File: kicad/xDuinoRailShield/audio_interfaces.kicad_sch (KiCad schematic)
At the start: 5 parts, among them J2 AudioJack2_Ground, J8 Conn_01x04, J9 Conn_01x05

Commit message: More busses added
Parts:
- renumbered C9 to C301, J2 to J301, J8 to J302, J9 to J303, RV1 to RV301
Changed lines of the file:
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@@
 		(dnp no)
 		(fields_autoplaced yes)
-		(property "Reference" "#PWR031"
+		(property "Reference" "#PWR0304"
 			(at 91.44 67.31 0)
 			(effects
@@
 			(project "xDuinoRailShield"
 				(path "/e63e39d7-6ac0-4ffd-8aa3-1841a4541b55/89db4163-62dc-424d-9343-e2bee6963b15"
-					(reference "#PWR031")
+					(reference "#PWR0304")
 					(unit 1)
 				)
@@
 		(on_board yes)
 		(dnp no)
-		(property "Reference" "RV1"
+		(property "Reference" "RV301"
 			(at 93.98 50.7999 0)
 			(effects
@@
 			(project "xDuinoRailShield"
 				(path "/e63e39d7-6ac0-4ffd-8aa3-1841a4541b55/89db4163-62dc-424d-9343-e2bee6963b15"
-					(reference "RV1")
+					(reference "RV301")
 					(unit 1)
 				)
@@
 		(on_board yes)
 		(dnp no)
-		(property "Reference" "J2"
+		(property "Reference" "J301"
 			(at 55.245 43.18 0)
 			(effects
@@
 			(project "xDuinoRailShield"
 				(path "/e63e39d7-6ac0-4ffd-8aa3-1841a4541b55/89db4163-62dc-424d-9343-e2bee6963b15"
-					(reference "J2")
+					(reference "J301")
 					(unit 1)
 				)
@@
 		(dnp no)
 		(fields_autoplaced yes)
-		(property "Reference" "#PWR029"
+		(property "Reference" "#PWR0301"
 			(at 55.88 67.31 0)
 			(effects
@@
 			(project "xDuinoRailShield"
 				(path "/e63e39d7-6ac0-4ffd-8aa3-1841a4541b55/89db4163-62dc-424d-9343-e2bee6963b15"
-					(reference "#PWR029")
+					(reference "#PWR0301")
 					(unit 1)
 				)
@@
 		(dnp no)
 		(fields_autoplaced yes)
-		(property "Reference" "#PWR030"
+		(property "Reference" "#PWR0302"
 			(at 73.66 50.8 0)
 			(effects
@@
 			(project "xDuinoRailShield"
 				(path "/e63e39d7-6ac0-4ffd-8aa3-1841a4541b55/89db4163-62dc-424d-9343-e2bee6963b15"
-					(reference "#PWR030")
+					(reference "#PWR0302")
 					(unit 1)
 				)
@@
 		(dnp no)
 		(fields_autoplaced yes)
-		(property "Reference" "#PWR038"
+		(property "Reference" "#PWR0303"
 			(at 78.74 123.19 0)
 			(effects
@@
 			(project "xDuinoRailShield"
 				(path "/e63e39d7-6ac0-4ffd-8aa3-1841a4541b55/89db4163-62dc-424d-9343-e2bee6963b15"
-					(reference "#PWR038")
+					(reference "#PWR0303")
 					(unit 1)
 				)
@@
 		(dnp no)
 		(fields_autoplaced yes)
-		(property "Reference" "#PWR039"
+		(property "Reference" "#PWR0305"
 			(at 157.48 125.73 0)
 			(effects
@@
 			(project "xDuinoRailShield"
 				(path "/e63e39d7-6ac0-4ffd-8aa3-1841a4541b55/89db4163-62dc-424d-9343-e2bee6963b15"
-					(reference "#PWR039")
+					(reference "#PWR0305")
 					(unit 1)
 				)
@@
 		(on_board yes)
 		(dnp no)
-		(property "Reference" "C9"
+		(property "Reference" "C301"
 			(at 83.439 44.45 90)
 			(effects
@@
 			(project "xDuinoRailShield"
 				(path "/e63e39d7-6ac0-4ffd-8aa3-1841a4541b55/89db4163-62dc-424d-9343-e2bee6963b15"
-					(reference "C9")
+					(reference "C301")
 					(unit 1)
 				)
@@
 		(on_board yes)
 		(dnp no)
-		(property "Reference" "J9"
+		(property "Reference" "J303"
 			(at 144.78 107.9499 0)
 			(effects
@@
 			(project "xDuinoRailShield"
 				(path "/e63e39d7-6ac0-4ffd-8aa3-1841a4541b55/89db4163-62dc-424d-9343-e2bee6963b15"
-					(reference "J9")
+					(reference "J303")
 					(unit 1)
 				)
@@
 		(on_board yes)
 		(dnp no)
-		(property "Reference" "J8"
+		(property "Reference" "J302"
 			(at 66.04 109.2201 0)
 			(effects
@@
 			(project "xDuinoRailShield"
 				(path "/e63e39d7-6ac0-4ffd-8aa3-1841a4541b55/89db4163-62dc-424d-9343-e2bee6963b15"
-					(reference "J8")
-					(unit 1)
-				)
+					(reference "J302")
+					(unit 1)
+				)

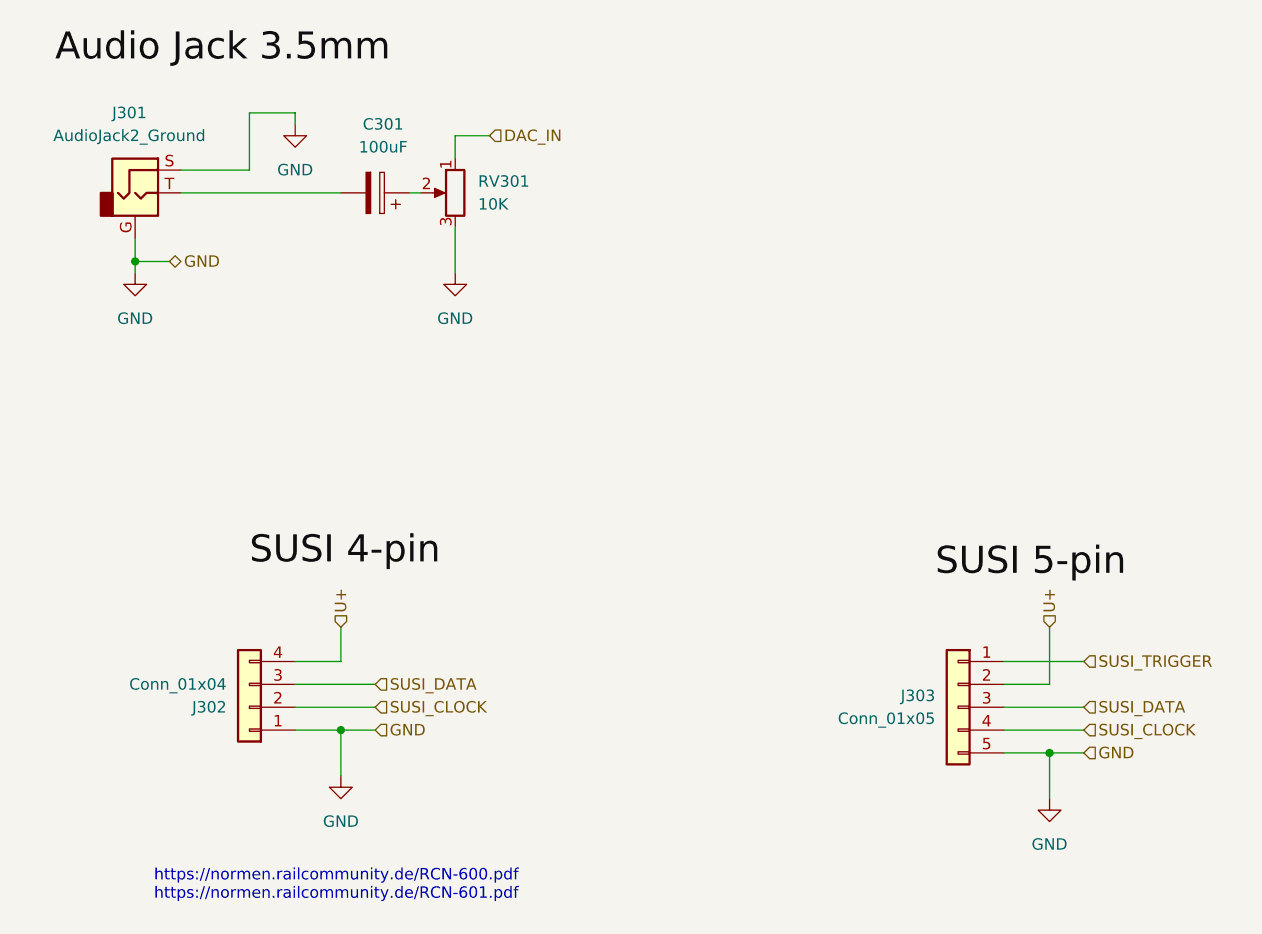
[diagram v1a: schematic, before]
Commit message: Draft of loco decoder
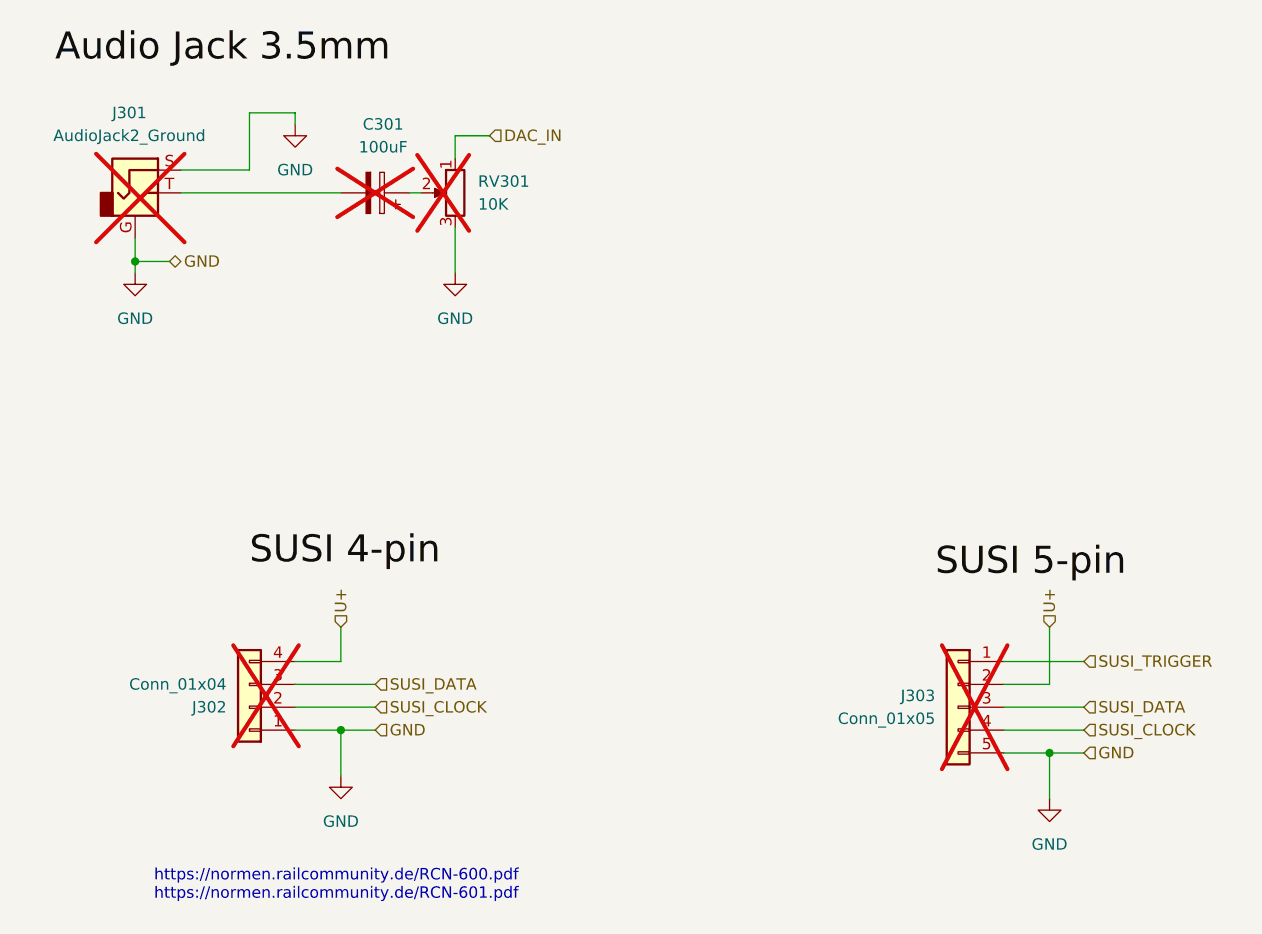
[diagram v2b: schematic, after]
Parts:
- C301, J301, J302, J303, RV301: now not fitted; now left out of the parts list
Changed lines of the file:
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@@
 		(mirror y)
 		(unit 1)
-		(exclude_from_sim no)
-		(in_bom yes)
-		(on_board yes)
-		(dnp no)
+		(exclude_from_sim yes)
+		(in_bom no)
+		(on_board no)
+		(dnp yes)
 		(property "Reference" "RV301"
 			(at 93.98 50.7999 0)
@@
 			)
 		)
+		(property "Field-1" ""
+			(at 91.44 52.07 0)
+			(effects
+				(font
+					(size 1.27 1.27)
+				)
+				(hide yes)
+			)
+		)
 		(pin "3"
 		)
@@
 		(at 55.88 52.07 0)
 		(unit 1)
-		(exclude_from_sim no)
-		(in_bom yes)
-		(on_board yes)
-		(dnp no)
+		(exclude_from_sim yes)
+		(in_bom no)
+		(on_board no)
+		(dnp yes)
 		(property "Reference" "J301"
 			(at 55.245 43.18 0)
@@
 		)
 		(property "Description" "Audio Jack, 2 Poles (Mono / TS), Grounded Sleeve"
+			(at 55.88 52.07 0)
+			(effects
+				(font
+					(size 1.27 1.27)
+				)
+				(hide yes)
+			)
+		)
+		(property "Field-1" ""
 			(at 55.88 52.07 0)
 			(effects
@@
 		(mirror x)
 		(unit 1)
-		(exclude_from_sim no)
-		(in_bom yes)
-		(on_board yes)
-		(dnp no)
+		(exclude_from_sim yes)
+		(in_bom no)
+		(on_board no)
+		(dnp yes)
 		(property "Reference" "C301"
 			(at 83.439 44.45 90)
@@
 		)
 		(property "Description" "Polarized capacitor"
+			(at 82.55 52.07 0)
+			(effects
+				(font
+					(size 1.27 1.27)
+				)
+				(hide yes)
+			)
+		)
+		(property "Field-1" ""
 			(at 82.55 52.07 0)
 			(effects
@@
 		(mirror y)
 		(unit 1)
-		(exclude_from_sim no)
-		(in_bom yes)
-		(on_board yes)
-		(dnp no)
+		(exclude_from_sim yes)
+		(in_bom no)
+		(on_board no)
+		(dnp yes)
 		(property "Reference" "J303"
 			(at 144.78 107.9499 0)
@@
 			)
 		)
+		(property "Field-1" ""
+			(at 147.32 109.22 0)
+			(effects
+				(font
+					(size 1.27 1.27)
+				)
+				(hide yes)
+			)
+		)
 		(pin "1"
 		)
@@
 		(at 68.58 109.22 180)
 		(unit 1)
-		(exclude_from_sim no)
-		(in_bom yes)
-		(on_board yes)
-		(dnp no)
+		(exclude_from_sim yes)
+		(in_bom no)
+		(on_board no)
+		(dnp yes)
 		(property "Reference" "J302"
 			(at 66.04 109.2201 0)
@@
 			(at 68.58 109.22 0)
 			(effects
+				(font
+					(size 1.27 1.27)
+				)
+				(hide yes)
+			)
+		)
+		(property "Field-1" ""
+			(at 68.58 109.22 0)
+			(effects

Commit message: A lot of fixes
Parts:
- renumbered C301 to C201, J301 to J201, J302 to J202, J303 to J203, RV301 to RV201
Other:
- note added: "Audio Jack 3.5mm"
- note added: "SUSI 4-pin"
- note added: "SUSI 5-pin"
- company: (none) -> Chatelain Engineering
- title: (none) -> DCC Bus Input
- moved on the sheet: J202
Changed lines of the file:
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@@
 	(generator_version "7.99")
 	(paper "A4")
+	(title_block
+		(title "DCC Bus Input")
+		(date "2024-01-03")
+		(rev "v0.1")
+		(company "Chatelain Engineering")
+	)
 	(junction
-		(at 78.74 111.76)
+		(at 71.12 113.03)
 		(diameter 0)
 		(color 0 0 0 0)
@@
 	(wire
 		(pts
-			(xy 78.74 100.33) (xy 78.74 104.14)
+			(xy 71.12 101.6) (xy 71.12 105.41)
 		)
 		(stroke
@@
 	(wire
 		(pts
-			(xy 78.74 111.76) (xy 78.74 116.84)
+			(xy 71.12 113.03) (xy 71.12 118.11)
 		)
 		(stroke
@@
 	(wire
 		(pts
-			(xy 78.74 111.76) (xy 82.55 111.76)
-		)
-		(stroke
-			(width 0)
-			(type default)
-		)
-	)
-	(wire
-		(pts
-			(xy 82.55 106.68) (xy 73.66 106.68)
-		)
-		(stroke
-			(width 0)
-			(type default)
-		)
-	)
-	(wire
-		(pts
-			(xy 73.66 104.14) (xy 78.74 104.14)
+			(xy 71.12 113.03) (xy 74.93 113.03)
+		)
+		(stroke
+			(width 0)
+			(type default)
+		)
+	)
+	(wire
+		(pts
+			(xy 74.93 107.95) (xy 66.04 107.95)
+		)
+		(stroke
+			(width 0)
+			(type default)
+		)
+	)
+	(wire
+		(pts
+			(xy 66.04 105.41) (xy 71.12 105.41)
 		)
 		(stroke
@@
 	(wire
 		(pts
-			(xy 82.55 109.22) (xy 73.66 109.22)
+			(xy 74.93 110.49) (xy 66.04 110.49)
 		)
 		(stroke
@@
 	(wire
 		(pts
-			(xy 73.66 111.76) (xy 78.74 111.76)
-		)
-		(stroke
-			(width 0)
-			(type default)
+			(xy 66.04 113.03) (xy 71.12 113.03)
+		)
+		(stroke
+			(width 0)
+			(type default)
+		)
+	)
+	(text "SUSI 5-pin"
+		(exclude_from_sim no)
+		(at 157.48 93.472 0)
+		(effects
+			(font
+				(size 3.048 3.048)
+			)
+		)
+	)
+	(text "SUSI 4-pin"
+		(exclude_from_sim no)
+		(at 73.66 93.726 0)
+		(effects
+			(font
+				(size 3.048 3.048)
+			)
 		)
 	)
 	(text "https://normen.railcommunity.de/RCN-600.pdf\nhttps://normen.railcommunity.de/RCN-601.pdf"
 		(exclude_from_sim no)
-		(at 78.232 129.032 0)
+		(at 70.612 130.302 0)
 		(effects
 			(font
@@
 		)
 	)
-	(label "Audio Jack 3.5mm"
-		(at 46.99 38.1 0)
-		(fields_autoplaced yes)
-		(effects
-			(font
-				(size 3 3)
-			)
-			(justify left bottom)
-		)
-	)
-	(label "SUSI 4-pin"
-		(at 68.58 93.98 0)
-		(fields_autoplaced yes)
-		(effects
-			(font
-				(size 3 3)
-			)
-			(justify left bottom)
-		)
-	)
-	(label "SUSI 5-pin"
-		(at 144.78 95.25 0)
-		(fields_autoplaced yes)
-		(effects
-			(font
-				(size 3 3)
-			)
-			(justify left bottom)
+	(text "Audio Jack 3.5mm"
+		(exclude_from_sim no)
+		(at 77.216 36.83 0)
+		(effects
+			(font
+				(size 3.048 3.048)
+			)
 		)
 	)
 	(hierarchical_label "SUSI_CLOCK"
 		(shape input)
-		(at 82.55 109.22 0)
+		(at 74.93 110.49 0)
 		(fields_autoplaced yes)
 		(effects
@@
 	(hierarchical_label "U+"
 		(shape input)
-		(at 78.74 100.33 90)
+		(at 71.12 101.6 90)
 		(fields_autoplaced yes)
 		(effects
@@
 	(hierarchical_label "GND"
 		(shape input)
-		(at 82.55 111.76 0)
+		(at 74.93 113.03 0)
 		(fields_autoplaced yes)
 		(effects
@@
 	(hierarchical_label "SUSI_DATA"
 		(shape input)
-		(at 82.55 106.68 0)
+		(at 74.93 107.95 0)
 		(fields_autoplaced yes)
 		(effects
@@
 		(dnp no)
 		(fields_autoplaced yes)
-		(property "Reference" "#PWR0304"
+		(property "Reference" "#PWR0204"
 			(at 91.44 67.31 0)
 			(effects
@@
 			(project "xDuinoRailShield"
 				(path "/e63e39d7-6ac0-4ffd-8aa3-1841a4541b55/89db4163-62dc-424d-9343-e2bee6963b15"
-					(reference "#PWR0304")
+					(reference "#PWR0204")
 					(unit 1)
 				)
@@
 		(on_board no)
 		(dnp yes)
-		(property "Reference" "RV301"
+		(property "Reference" "RV201"
 			(at 93.98 50.7999 0)
 			(effects
@@
 			(project "xDuinoRailShield"
 				(path "/e63e39d7-6ac0-4ffd-8aa3-1841a4541b55/89db4163-62dc-424d-9343-e2bee6963b15"
-					(reference "RV301")
+					(reference "RV201")
 					(unit 1)
 				)
@@
 		(on_board no)
 		(dnp yes)
-		(property "Reference" "J301"
+		(property "Reference" "J201"
 			(at 55.245 43.18 0)
 			(effects
@@
 			(project "xDuinoRailShield"
 				(path "/e63e39d7-6ac0-4ffd-8aa3-1841a4541b55/89db4163-62dc-424d-9343-e2bee6963b15"
-					(reference "J301")
+					(reference "J201")
 					(unit 1)
 				)
@@
 		(dnp no)
 		(fields_autoplaced yes)
-		(property "Reference" "#PWR0301"
+		(property "Reference" "#PWR0201"
 			(at 55.88 67.31 0)
 			(effects
@@
 			(project "xDuinoRailShield"
 				(path "/e63e39d7-6ac0-4ffd-8aa3-1841a4541b55/89db4163-62dc-424d-9343-e2bee6963b15"
-					(reference "#PWR0301")
+					(reference "#PWR0201")
 					(unit 1)
 				)
@@
 		(dnp no)
 		(fields_autoplaced yes)
-		(property "Reference" "#PWR0302"
+		(property "Reference" "#PWR0202"
 			(at 73.66 50.8 0)
 			(effects
@@
 			(project "xDuinoRailShield"
 				(path "/e63e39d7-6ac0-4ffd-8aa3-1841a4541b55/89db4163-62dc-424d-9343-e2bee6963b15"
-					(reference "#PWR0302")
+					(reference "#PWR0202")
 					(unit 1)
 				)
@@
 	(symbol
 		(lib_id "power:GND")
-		(at 78.74 116.84 0)
+		(at 71.12 118.11 0)
 		(unit 1)
 		(exclude_from_sim no)
@@
 		(dnp no)
 		(fields_autoplaced yes)
-		(property "Reference" "#PWR0303"
-			(at 78.74 123.19 0)
+		(property "Reference" "#PWR0203"
+			(at 71.12 124.46 0)
 			(effects
 				(font
@@
 		)
 		(property "Value" "GND"
-			(at 78.74 121.92 0)
+			(at 71.12 123.19 0)
 			(effects
 				(font
@@
 		)
 		(property "Footprint" ""
-			(at 78.74 116.84 0)
+			(at 71.12 118.11 0)
 			(effects
 				(font
@@
 		)
 		(property "Datasheet" ""
-			(at 78.74 116.84 0)
+			(at 71.12 118.11 0)
 			(effects
 				(font
@@
 		)
 		(property "Description" "Power symbol creates a global label with name \"GND\" , ground"
-			(at 78.74 116.84 0)
+			(at 71.12 118.11 0)
 			(effects
 				(font
@@
 			(project "xDuinoRailShield"
 				(path "/e63e39d7-6ac0-4ffd-8aa3-1841a4541b55/89db4163-62dc-424d-9343-e2bee6963b15"
-					(reference "#PWR0303")
+					(reference "#PWR0203")
 					(unit 1)
 				)
@@
 		(dnp no)
 		(fields_autoplaced yes)
-		(property "Reference" "#PWR0305"
+		(property "Reference" "#PWR0205"
 			(at 157.48 125.73 0)
 			(effects
@@
 			(project "xDuinoRailShield"
 				(path "/e63e39d7-6ac0-4ffd-8aa3-1841a4541b55/89db4163-62dc-424d-9343-e2bee6963b15"
-					(reference "#PWR0305")
+					(reference "#PWR0205")
 					(unit 1)
 				)
@@
 		(on_board no)
 		(dnp yes)
-		(property "Reference" "C301"
+		(property "Reference" "C201"
 			(at 83.439 44.45 90)
 			(effects
@@
 			(project "xDuinoRailShield"
 				(path "/e63e39d7-6ac0-4ffd-8aa3-1841a4541b55/89db4163-62dc-424d-9343-e2bee6963b15"
-					(reference "C301")
+					(reference "C201")
 					(unit 1)
 				)
@@
 		(on_board no)
 		(dnp yes)
-		(property "Reference" "J303"
+		(property "Reference" "J203"
 			(at 144.78 107.9499 0)
 			(effects
@@
 			(project "xDuinoRailShield"
 				(path "/e63e39d7-6ac0-4ffd-8aa3-1841a4541b55/89db4163-62dc-424d-9343-e2bee6963b15"
-					(reference "J303")
+					(reference "J203")
 					(unit 1)
 				)
@@
 	(symbol
 		(lib_id "Connector_Generic:Conn_01x04")
-		(at 68.58 109.22 180)
+		(at 60.96 110.49 180)
 		(unit 1)
 		(exclude_from_sim yes)
@@
 		(on_board no)
 		(dnp yes)
-		(property "Reference" "J302"
-			(at 66.04 109.2201 0)
+		(property "Reference" "J202"
+			(at 58.42 110.4901 0)
 			(effects
 				(font
@@
 		)
 		(property "Value" "Conn_01x04"
-			(at 66.04 106.6801 0)
+			(at 58.42 107.9501 0)
 			(effects
 				(font
@@
 		)
 		(property "Footprint" ""
-			(at 68.58 109.22 0)
+			(at 60.96 110.49 0)
 			(effects
 				(font
@@
 		)
 		(property "Datasheet" "~"
-			(at 68.58 109.22 0)
+			(at 60.96 110.49 0)
 			(effects
 				(font
@@
 		)
 		(property "Description" "Generic connector, single row, 01x04, script generated (kicad-library-utils/schlib/autogen/connector/)"
-			(at 68.58 109.22 0)
+			(at 60.96 110.49 0)
 			(effects
 				(font
@@
 		)
 		(property "Field-1" ""
-			(at 68.58 109.22 0)
+			(at 60.96 110.49 0)
 			(effects
 				(font
@@
 			(project "xDuinoRailShield"
 				(path "/e63e39d7-6ac0-4ffd-8aa3-1841a4541b55/89db4163-62dc-424d-9343-e2bee6963b15"
-					(reference "J302")
+					(reference "J202")
 					(unit 1)
 				)

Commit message: Refactoring & Sound
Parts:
- added U201: MCP4725xxx-xCH, Package_TO_SOT_SMD:SOT-23-6_Handsoldering, symbol Analog_DAC:MCP4725xxx-xCH
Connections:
- net GND: now also U201.2 (VSS)
- new net +3V3: U201.3 (VDD), U201.6 (A0)
- new net I2C0: U201.5 (SCL)
- new net I2C1: U201.4 (SDA)
- new net SPEAKER0: U201.1 (VOUT)
